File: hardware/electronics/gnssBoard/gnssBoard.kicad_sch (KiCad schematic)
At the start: 48 parts, among them J1 Standoff, J2 M.2_E_Key_PCB_Edge, Q1 DMG1013TQ-7, U1 AP7361E, U2 TXS0104VxRUTR, U3 ZED-F9P, U4 OPA344

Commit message: netclass
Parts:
- JP2: symbol lib_sch:Jumper_2_Bridged -> lib_sch:Jumper_2_Bridged_1
- TP1, TP2, TP4, TP5, TP6, TP7, TP9: symbol lib_sch:Testpoint -> lib_sch:Testpoint_1
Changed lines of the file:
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@@
 	(label "TX_RDY"
 		(at 161.29 149.86 180)
-		(fields_autoplaced yes)
 		(effects
 			(font
@@
 	(label "ANT_IN"
 		(at 36.83 137.16 180)
-		(fields_autoplaced yes)
 		(effects
 			(font
@@
 	(label "ANT_SHORT_N"
 		(at 48.26 203.2 180)
-		(fields_autoplaced yes)
 		(effects
 			(font
@@
 	(label "ZED_RXD_3V3"
 		(at 88.9 176.53 0)
-		(fields_autoplaced yes)
 		(effects
 			(font
@@
 	(label "PPS"
 		(at 88.9 157.48 0)
-		(fields_autoplaced yes)
 		(effects
 			(font
@@
 	(label "RESET_N"
 		(at 180.34 22.86 0)
-		(fields_autoplaced yes)
 		(effects
 			(font
@@
 	(label "HOST_D-"
 		(at 180.34 58.42 0)
-		(fields_autoplaced yes)
 		(effects
 			(font
@@
 	(label "TX_RDY"
 		(at 251.46 33.02 180)
-		(fields_autoplaced yes)
 		(effects
 			(font
@@
 	(label "ZED_D-"
 		(at 88.9 170.18 0)
-		(fields_autoplaced yes)
 		(effects
 			(font
@@
 	(label "HOST_D+"
 		(at 180.34 55.88 0)
-		(fields_autoplaced yes)
 		(effects
 			(font
@@
 	(label "RESET_N"
 		(at 88.9 137.16 0)
-		(fields_autoplaced yes)
 		(effects
 			(font
@@
 	(label "ZED_RXD_1V8"
 		(at 53.34 87.63 0)
-		(fields_autoplaced yes)
 		(effects
 			(font
@@
 	(label "RTK_STAT"
 		(at 259.08 88.9 180)
-		(fields_autoplaced yes)
 		(effects
 			(font
@@
 	(label "ANT_SHORT_N"
 		(at 88.9 153.67 0)
-		(fields_autoplaced yes)
 		(effects
 			(font
@@
 	(label "SCL_3V3"
 		(at 99.06 92.71 180)
-		(fields_autoplaced yes)
 		(effects
 			(font
@@
 	(label "GEOFENCE_STAT"
 		(at 167.64 137.16 180)
-		(fields_autoplaced yes)
 		(effects
 			(font
@@
 	(label "ZED_TXD_1V8"
 		(at 255.27 76.2 180)
-		(fields_autoplaced yes)
 		(effects
 			(font
@@
 	(label "EXTINT"
 		(at 88.9 142.24 0)
-		(fields_autoplaced yes)
 		(effects
 			(font
@@
 	(label "SDA_1V8"
 		(at 53.34 90.17 0)
-		(fields_autoplaced yes)
 		(effects
 			(font
@@
 	(label "ZED_D+"
 		(at 88.9 167.64 0)
-		(fields_autoplaced yes)
 		(effects
 			(font
@@
 	(label "ANT_OFF"
 		(at 48.26 162.56 180)
-		(fields_autoplaced yes)
 		(effects
 			(font
@@
 	(label "ANT_DET"
 		(at 88.9 148.59 0)
-		(fields_autoplaced yes)
 		(effects
 			(font
@@
 	(label "ZED_TXD_3V3"
 		(at 88.9 173.99 0)
-		(fields_autoplaced yes)
 		(effects
 			(font
@@
 	(label "SDA_3V3"
 		(at 88.9 180.34 0)
-		(fields_autoplaced yes)
 		(effects
 			(font
@@
 	(label "GEOFENCE_STAT"
 		(at 259.08 86.36 180)
-		(fields_autoplaced yes)
 		(effects
 			(font
@@
 	(label "ZED_TXD_3V3"
 		(at 99.06 85.09 180)
-		(fields_autoplaced yes)
 		(effects
 			(font
@@
 	(label "ZED_TXD_1V8"
 		(at 53.34 85.09 0)
-		(fields_autoplaced yes)
 		(effects
 			(font
@@
 	(label "HOST_D+"
 		(at 72.39 166.37 0)
-		(fields_autoplaced yes)
 		(effects
 			(font
@@
 	(label "EXTINT"
 		(at 251.46 30.48 180)
-		(fields_autoplaced yes)
 		(effects
 			(font
@@
 	(label "SDA_3V3"
 		(at 99.06 90.17 180)
-		(fields_autoplaced yes)
 		(effects
 			(font
@@
 	(label "RTK_STAT"
 		(at 167.64 139.7 180)
-		(fields_autoplaced yes)
 		(effects
 			(font
@@
 	(label "ANT_DET"
 		(at 48.26 190.5 180)
-		(fields_autoplaced yes)
 		(effects
 			(font
@@
 	(label "ANT_OFF"
 		(at 88.9 151.13 0)
-		(fields_autoplaced yes)
 		(effects
 			(font
@@
 	(label "ZED_RXD_1V8"
 		(at 255.27 73.66 180)
-		(fields_autoplaced yes)
 		(effects
 			(font
@@
 	(label "SCL_1V8"
 		(at 251.46 40.64 180)
-		(fields_autoplaced yes)
 		(effects
 			(font
@@
 	(label "SCL_3V3"
 		(at 88.9 182.88 0)
-		(fields_autoplaced yes)
 		(effects
 			(font
@@
 	(label "ZED_RXD_3V3"
 		(at 99.06 87.63 180)
-		(fields_autoplaced yes)
 		(effects
 			(font
@@
 	(label "HOST_D-"
 		(at 72.39 171.45 0)
-		(fields_autoplaced yes)
 		(effects
 			(font
@@
 	(label "RF_IN"
 		(at 57.15 137.16 180)
-		(fields_autoplaced yes)
 		(effects
 			(font
@@
 	(label "SCL_1V8"
 		(at 53.34 92.71 0)
-		(fields_autoplaced yes)
 		(effects
 			(font
@@
 	(label "SDA_1V8"
 		(at 251.46 38.1 180)
-		(fields_autoplaced yes)
 		(effects
 			(font
@@
 	(label "RF_IN"
 		(at 88.9 146.05 0)
-		(fields_autoplaced yes)
 		(effects
 			(font
@@
 	(label "PPS"
 		(at 251.46 27.94 180)
-		(fields_autoplaced yes)
 		(effects
 			(font
@@
 		)
 	)
+	(netclass_flag ""
+		(length 2.54)
+		(shape round)
+		(at 88.9 146.05 90)
+		(effects
+			(font
+				(size 1.27 1.27)
+			)
+			(justify left bottom)
+		)
+		(property "Netclass" "GNSS RF"
+			(at 85.09 146.05 0)
+			(effects
+				(font
+					(size 1.27 1.27)
+					(italic yes)
+				)
+				(justify right)
+			)
+		)
+	)
+	(netclass_flag ""
+		(length 2.54)
+		(shape round)
+		(at 57.15 137.16 270)
+		(effects
+			(font
+				(size 1.27 1.27)
+			)
+			(justify right bottom)
+		)
+		(property "Netclass" "GNSS RF"
+			(at 60.96 137.16 0)
+			(effects
+				(font
+					(size 1.27 1.27)
+					(italic yes)
+				)
+				(justify left)
+			)
+		)
+	)
+	(netclass_flag ""
+		(length 2.54)
+		(shape round)
+		(at 39.37 137.16 0)
+		(effects
+			(font
+				(size 1.27 1.27)
+			)
+			(justify left bottom)
+		)
+		(property "Netclass" "GNSS RF"
+			(at 39.37 133.35 0)
+			(effects
+				(font
+					(size 1.27 1.27)
+					(italic yes)
+				)
+				(justify bottom)
+			)
+		)
+	)
+	(netclass_flag ""
+		(length 2.54)
+		(shape diamond)
+		(at 72.39 166.37 90)
+		(effects
+			(font
+				(size 1.27 1.27)
+			)
+			(justify left bottom)
+		)
+		(property "Netclass" "USB Diff Pair"
+			(at 68.58 166.37 0)
+			(effects
+				(font
+					(size 1.27 1.27)
+					(italic yes)
+				)
+				(justify right)
+			)
+		)
+	)
+	(netclass_flag ""
+		(length 2.54)
+		(shape diamond)
+		(at 99.06 170.18 0)
+		(effects
+			(font
+				(size 1.27 1.27)
+			)
+			(justify left bottom)
+		)
+		(property "Netclass" "USB Diff Pair"
+			(at 99.06 163.83 0)
+			(effects
+				(font
+					(size 1.27 1.27)
+					(italic yes)
+				)
+				(justify right)
+			)
+		)
+	)
+	(netclass_flag ""
+		(length 2.54)
+		(shape diamond)
+		(at 99.06 167.64 0)
+		(effects
+			(font
+				(size 1.27 1.27)
+			)
+			(justify left bottom)
+		)
+		(property "Netclass" "USB Diff Pair"
+			(at 99.06 162.052 0)
+			(effects
+				(font
+					(size 1.27 1.27)
+					(italic yes)
+				)
+				(justify right)
+			)
+		)
+	)
+	(netclass_flag ""
+		(length 2.54)
+		(shape diamond)
+		(at 72.39 171.45 90)
+		(effects
+			(font
+				(size 1.27 1.27)
+			)
+			(justify left bottom)
+		)
+		(property "Netclass" "USB Diff Pair"
+			(at 68.58 171.45 0)
+			(effects
+				(font
+					(size 1.27 1.27)
+					(italic yes)
+				)
+				(justify right)
+			)
+		)
+	)
 	(symbol
 		(lib_id "lib_sch:VSS")
@@
 	)
 	(symbol
-		(lib_id "DS-Power:PWR_FLAG")
+		(lib_id "lib_sch:PWR_FLAG")
 		(at 63.5 48.26 180)
 		(unit 1)
@@
 	(symbol
 		(lib_name "Testpoint_1")
-		(lib_id "lib_sch:Testpoint")
+		(lib_id "lib_sch:Testpoint_1")
 		(at 44.45 82.55 0)
 		(unit 1)
@@
 	(symbol
 		(lib_name "Testpoint_1")
-		(lib_id "lib_sch:Testpoint")
+		(lib_id "lib_sch:Testpoint_1")
 		(at 85.09 154.94 0)
 		(unit 1)
@@
 	(symbol
 		(lib_name "Testpoint_1")
-		(lib_id "lib_sch:Testpoint")
+		(lib_id "lib_sch:Testpoint_1")
 		(at 87.63 27.94 0)
 		(unit 1)
@@
 	(symbol
 		(lib_name "Testpoint_1")
-		(lib_id "lib_sch:Testpoint")
+		(lib_id "lib_sch:Testpoint_1")
 		(at 38.1 82.55 0)
 		(unit 1)
@@
 	(symbol
 		(lib_name "Testpoint_1")
-		(lib_id "lib_sch:Testpoint")
+		(lib_id "lib_sch:Testpoint_1")
 		(at 50.8 82.55 0)
 		(unit 1)
@@
 	(symbol
 		(lib_name "Jumper_2_Bridged_1")
-		(lib_id "lib_sch:Jumper_2_Bridged")
+		(lib_id "lib_sch:Jumper_2_Bridged_1")
 		(at 64.77 157.48 0)
 		(mirror y)
@@
 	(symbol
 		(lib_name "Testpoint_1")
-		(lib_id "lib_sch:Testpoint")
+		(lib_id "lib_sch:Testpoint_1")
 		(at 31.75 82.55 0)
 		(unit 1)
@@
 	)
 	(symbol
-		(lib_id "DS-Power:PWR_FLAG")
+		(lib_id "lib_sch:PWR_FLAG")
 		(at 50.8 30.48 90)
 		(unit 1)
@@
 	(symbol
 		(lib_name "Testpoint_1")
-		(lib_id "lib_sch:Testpoint")
+		(lib_id "lib_sch:Testpoint_1")
 		(at 62.23 27.94 0)
 		(unit 1)

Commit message: upgraded to v9
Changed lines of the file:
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@@
 (kicad_sch
-	(version 20231120)
+	(version 20250114)
 	(generator "eeschema")
-	(generator_version "8.0")
+	(generator_version "9.0")
 	(paper "USLetter")
 	(title_block
@@
 		(comment 3 "2025")
 	)
+	(text "Place close to pin 38"
+		(exclude_from_sim no)
+		(at 215.9 156.845 0)
+		(effects
+			(font
+				(size 1.27 1.27)
+			)
+		)
+	)
+	(text "Place close to pins 33/34"
+		(exclude_from_sim no)
+		(at 190.5 156.845 0)
+		(effects
+			(font
+				(size 1.27 1.27)
+			)
+		)
+	)
+	(text "+1V8/+3V3 Level Shifter"
+		(exclude_from_sim no)
+		(at 10.16 65.405 0)
+		(effects
+			(font
+				(face "KiCad Font")
+				(size 1.27 1.27)
+				(thickness 0.254)
+				(bold yes)
+				(italic yes)
+			)
+			(justify left)
+		)
+	)
+	(text "ZED-F9P GNSS Receiver"
+		(exclude_from_sim no)
+		(at 10.16 116.205 0)
+		(effects
+			(font
+				(face "KiCad Font")
+				(size 1.27 1.27)
+				(thickness 0.254)
+				(bold yes)
+				(italic yes)
+			)
+			(justify left)
+		)
+	)
+	(text "+1V8 Voltage Regulator"
+		(exclude_from_sim no)
+		(at 10.16 11.43 0)
+		(effects
+			(font
+				(face "KiCad Font")
+				(size 1.27 1.27)
+				(thickness 0.254)
+				(bold yes)
+				(italic yes)
+			)
+			(justify left)
+		)
+	)
+	(text "Pullup for I2C"
+		(exclude_from_sim no)
+		(at 92.075 189.865 0)
+		(effects
+			(font
+				(size 1.27 1.27)
+			)
+		)
+	)
+	(text "M.2 E-Key Edge Card Connector"
+		(exclude_from_sim no)
+		(at 140.335 11.43 0)
+		(effects
+			(font
+				(face "KiCad Font")
+				(size 1.27 1.27)
+				(thickness 0.254)
+				(bold yes)
+				(italic yes)
+			)
+			(justify left)
+		)
+	)
+	(text_box "Antenna Feedline Impedance: 50 Ohm\nFor 0.8mm thickness, tracewidth is 0.2565mm"
+		(exclude_from_sim no)
+		(at 53.34 118.11 0)
+		(size 39.37 8.89)
+		(margins 0.9525 0.9525 0.9525 0.9525)
+		(stroke
+			(width 0)
+			(type default)
+		)
+		(fill
+			(type none)
+		)
+		(effects
+			(font
+				(size 1.27 1.27)
+			)
+			(justify left top)
+		)
+	)
 	(junction
 		(at 87.63 30.48)
@@
 		)
 	)
-	(text_box "Antenna Feedline Impedance: 50 Ohm\nFor 0.8mm thickness, tracewidth is 0.2565mm"
-		(exclude_from_sim no)
-		(at 53.34 118.11 0)
-		(size 39.37 8.89)
-		(stroke
-			(width 0)
-			(type default)
-		)
-		(fill
-			(type none)
-		)
-		(effects
-			(font
-				(size 1.27 1.27)
-			)
-			(justify left top)
-		)
-	)
-	(text "Place close to pin 38"
-		(exclude_from_sim no)
-		(at 215.9 156.845 0)
-		(effects
-			(font
-				(size 1.27 1.27)
-			)
-		)
-	)
-	(text "Place close to pins 33/34"
-		(exclude_from_sim no)
-		(at 190.5 156.845 0)
-		(effects
-			(font
-				(size 1.27 1.27)
-			)
-		)
-	)
-	(text "+1V8/+3V3 Level Shifter"
-		(exclude_from_sim no)
-		(at 10.16 65.405 0)
-		(effects
-			(font
-				(face "KiCad Font")
-				(size 1.27 1.27)
-				(thickness 0.254)
-				(bold yes)
-				(italic yes)
-			)
-			(justify left)
-		)
-	)
-	(text "ZED-F9P GNSS Receiver"
-		(exclude_from_sim no)
-		(at 10.16 116.205 0)
-		(effects
-			(font
-				(face "KiCad Font")
-				(size 1.27 1.27)
-				(thickness 0.254)
-				(bold yes)
-				(italic yes)
-			)
-			(justify left)
-		)
-	)
-	(text "+1V8 Voltage Regulator"
-		(exclude_from_sim no)
-		(at 10.16 11.43 0)
-		(effects
-			(font
-				(face "KiCad Font")
-				(size 1.27 1.27)
-				(thickness 0.254)
-				(bold yes)
-				(italic yes)
-			)
-			(justify left)
-		)
-	)
-	(text "Pullup for I2C"
-		(exclude_from_sim no)
-		(at 92.075 189.865 0)
-		(effects
-			(font
-				(size 1.27 1.27)
-			)
-		)
-	)
-	(text "M.2 E-Key Edge Card Connector"
-		(exclude_from_sim no)
-		(at 140.335 11.43 0)
-		(effects
-			(font
-				(face "KiCad Font")
-				(size 1.27 1.27)
-				(thickness 0.254)
-				(bold yes)
-				(italic yes)
-			)
-			(justify left)
-		)
-	)
 	(label "TX_RDY"
 		(at 161.29 149.86 180)
@@
 		)
 	)
+	(embedded_fonts no)
 )

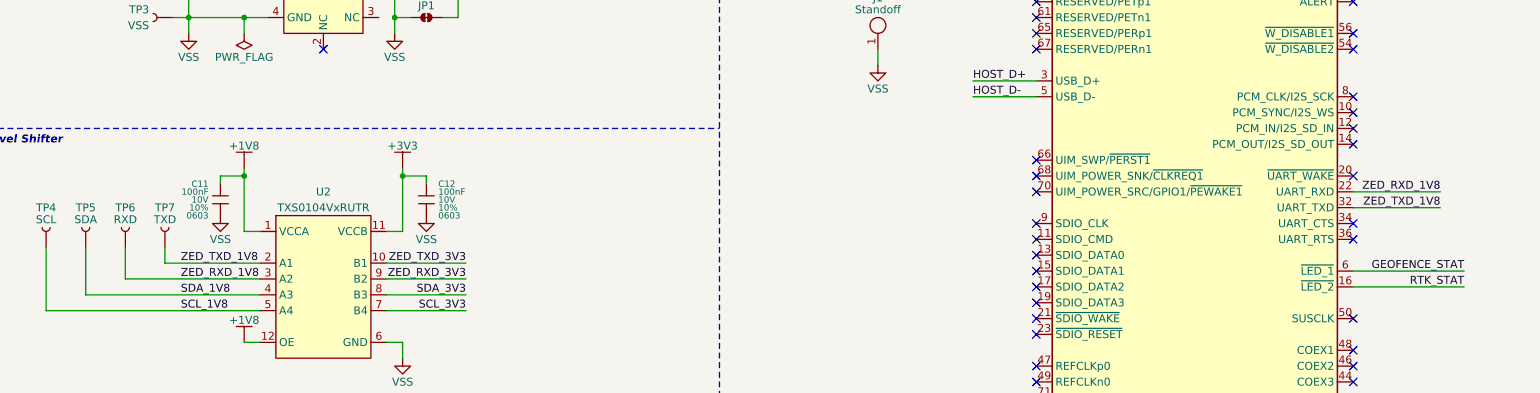
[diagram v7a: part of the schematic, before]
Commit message: fixed RXD/TXD
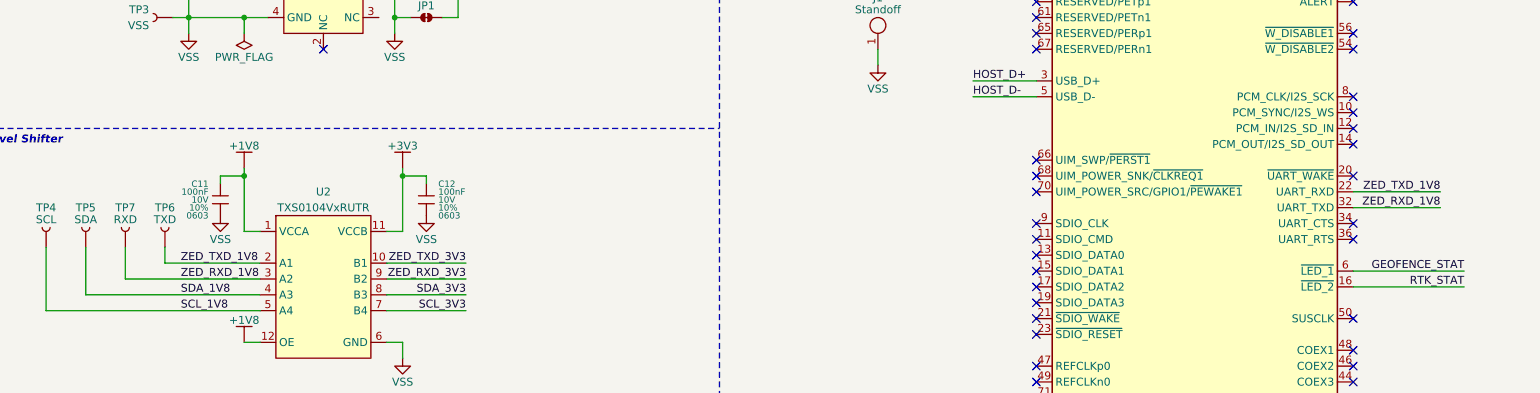
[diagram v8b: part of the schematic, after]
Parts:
- TP6: value RXD -> TXD
- TP7: value TXD -> RXD
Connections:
- net ZED_RXD_1V8: now also J2.32 (UART_TXD), TP7.1; no longer J2.22 (UART_RXD), TP6.1
- net ZED_TXD_1V8: now also J2.22 (UART_RXD), TP6.1; no longer J2.32 (UART_TXD), TP7.1
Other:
- moved on the sheet: TP6, TP7
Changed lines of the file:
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@@
 	(title_block
 		(title "U-bolx ZED-F9P M.2 E-Key")
-		(date "2025-01-13")
-		(rev "01")
+		(date "2025-03-16")
+		(rev "1.1")
 		(comment 2 "PROTOTYPE")
 		(comment 3 "2025")
@@
 	(wire
 		(pts
+			(xy 44.45 82.55) (xy 44.45 87.63)
+		)
+		(stroke
+			(width 0)
+			(type default)
+		)
+	)
+	(wire
+		(pts
 			(xy 241.3 142.24) (xy 241.3 144.78)
 		)
@@
 	(wire
 		(pts
-			(xy 50.8 82.55) (xy 50.8 85.09)
-		)
-		(stroke
-			(width 0)
-			(type default)
-		)
-	)
-	(wire
-		(pts
 			(xy 88.9 69.85) (xy 88.9 71.12)
 		)
@@
 	(wire
 		(pts
+			(xy 50.8 82.55) (xy 50.8 85.09)
+		)
+		(stroke
+			(width 0)
+			(type default)
+		)
+	)
+	(wire
+		(pts
 			(xy 241.3 38.1) (xy 251.46 38.1)
 		)
@@
 	(wire
 		(pts
-			(xy 44.45 82.55) (xy 44.45 87.63)
-		)
-		(stroke
-			(width 0)
-			(type default)
-		)
-	)
-	(wire
-		(pts
 			(xy 63.5 97.79) (xy 66.04 97.79)
 		)
@@
 		)
 	)
+	(label "ZED_TXD_1V8"
+		(at 255.27 73.66 180)
+		(effects
+			(font
+				(size 1.27 1.27)
+			)
+			(justify right bottom)
+		)
+	)
 	(label "RESET_N"
 		(at 180.34 22.86 0)
@@
 		)
 	)
-	(label "ZED_TXD_1V8"
-		(at 255.27 76.2 180)
-		(effects
-			(font
-				(size 1.27 1.27)
-			)
-			(justify right bottom)
-		)
-	)
 	(label "EXTINT"
 		(at 88.9 142.24 0)
@@
 		)
 	)
-	(label "ZED_RXD_1V8"
-		(at 255.27 73.66 180)
+	(label "SCL_1V8"
+		(at 251.46 40.64 180)
 		(effects
 			(font
@@
 		)
 	)
-	(label "SCL_1V8"
-		(at 251.46 40.64 180)
+	(label "ZED_RXD_1V8"
+		(at 255.27 76.2 180)
 		(effects
 			(font
@@
 		(lib_name "Testpoint_1")
 		(lib_id "lib_sch:Testpoint_1")
-		(at 44.45 82.55 0)
+		(at 50.8 82.55 0)
 		(unit 1)
 		(exclude_from_sim no)
@@
 		(fields_autoplaced yes)
 		(property "Reference" "TP6"
-			(at 44.45 76.2 0)
+			(at 50.8 76.2 0)
 			(do_not_autoplace yes)
 			(effects
@@
 			)
 		)
-		(property "Value" "RXD"
-			(at 44.45 78.105 0)
+		(property "Value" "TXD"
+			(at 50.8 78.105 0)
 			(do_not_autoplace yes)
 			(effects
@@
 		)
 		(property "Footprint" "lib_fp:TP_1mm"
-			(at 44.45 80.01 90)
+			(at 50.8 80.01 90)
 			(effects
 				(font
@@
 		)
 		(property "Datasheet" ""
-			(at 44.45 80.01 90)
+			(at 50.8 80.01 90)
 			(effects
 				(font
@@
 		)
 		(property "Description" ""
-			(at 44.45 80.01 90)
+			(at 50.8 80.01 90)
 			(effects
 				(font
@@
 		)
 		(property "Manufacturer" ""
-			(at 44.45 80.01 90)
+			(at 50.8 80.01 90)
 			(effects
 				(font
@@
 		)
 		(property "MPN" ""
-			(at 44.45 80.01 90)
+			(at 50.8 80.01 90)
 			(effects
 				(font
@@
 		)
 		(property "DKPN" ""
-			(at 44.45 80.01 90)
+			(at 50.8 80.01 90)
 			(effects
 				(font
@@
 		(lib_name "Testpoint_1")
 		(lib_id "lib_sch:Testpoint_1")
-		(at 50.8 82.55 0)
+		(at 44.45 82.55 0)
 		(unit 1)
 		(exclude_from_sim no)
@@
 		(fields_autoplaced yes)
 		(property "Reference" "TP7"
-			(at 50.8 76.2 0)
+			(at 44.45 76.2 0)
 			(do_not_autoplace yes)
 			(effects
@@
 			)
 		)
-		(property "Value" "TXD"
-			(at 50.8 78.105 0)
+		(property "Value" "RXD"
+			(at 44.45 78.105 0)
 			(do_not_autoplace yes)
 			(effects
@@
 		)
 		(property "Footprint" "lib_fp:TP_1mm"
-			(at 50.8 80.01 90)
+			(at 44.45 80.01 90)
 			(effects
 				(font
@@
 		)
 		(property "Datasheet" ""
-			(at 50.8 80.01 90)
+			(at 44.45 80.01 90)
 			(effects
 				(font
@@
 		)
 		(property "Description" ""
-			(at 50.8 80.01 90)
+			(at 44.45 80.01 90)
 			(effects
 				(font
@@
 		)
 		(property "Manufacturer" ""
-			(at 50.8 80.01 90)
+			(at 44.45 80.01 90)
 			(effects
 				(font
@@
 		)
 		(property "MPN" ""
-			(at 50.8 80.01 90)
+			(at 44.45 80.01 90)
 			(effects
 				(font
@@
 		)
 		(property "DKPN" ""
-			(at 50.8 80.01 90)
+			(at 44.45 80.01 90)
 			(effects
 				(font
